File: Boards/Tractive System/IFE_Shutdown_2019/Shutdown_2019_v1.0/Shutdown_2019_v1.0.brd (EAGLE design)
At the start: 88.9 x 76.2 mm, 194 parts, among them Q1 DMN6140L-7, Q10 DMN6140L-7, Q11 DMP3099L-7, Q12 IRLML6346PBF, Q13 IRLML6346PBF, Q14 IRLML6346PBF, Q15 DMP3099L-7, Q16 DMN6140L-7, Q17 IRLML6346PBF, Q18 DMN6140L-7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

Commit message: Done with safety initial layout
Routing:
- net GND: track 0.00 -> 62.7 mm, vias 0 -> 128
- net +5V: track 241.0 -> 270.3 mm, vias 25 -> 27
- net +3V3: track 194.4 -> 219.4 mm, vias 13 -> 17
- net BRAKE_PRESSURE_F: track 4.22 -> 17.1 mm, vias 0 -> 2
- net DEBUG_TC: track 14.3 -> 15.1 mm
- net CURRENT_SENSE_F: track 35.2 -> 36.0 mm
- net BSPD_OC: track 13.2 -> 13.8 mm
- added copper zone on layer 1, net GND
- added copper zone on layer 16, net GND

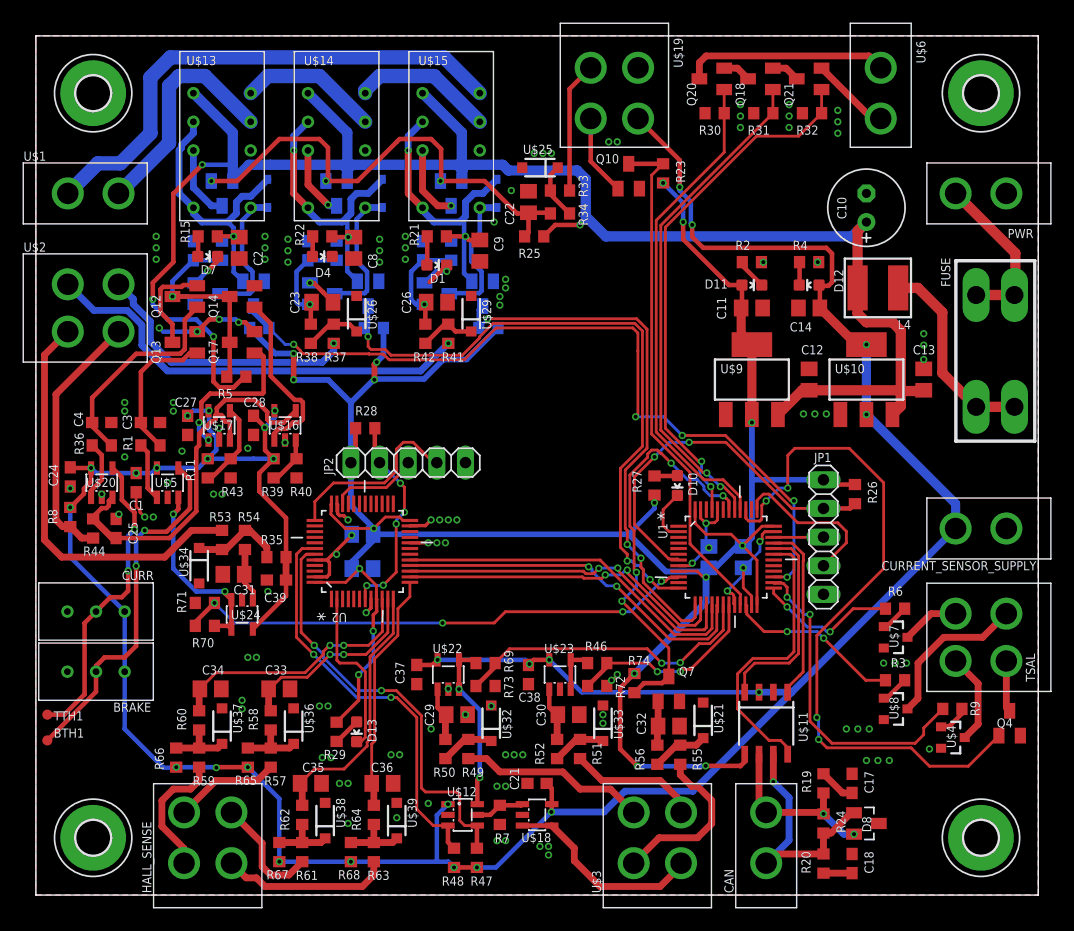
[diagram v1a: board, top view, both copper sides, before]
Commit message: Added rounded edges + Silk
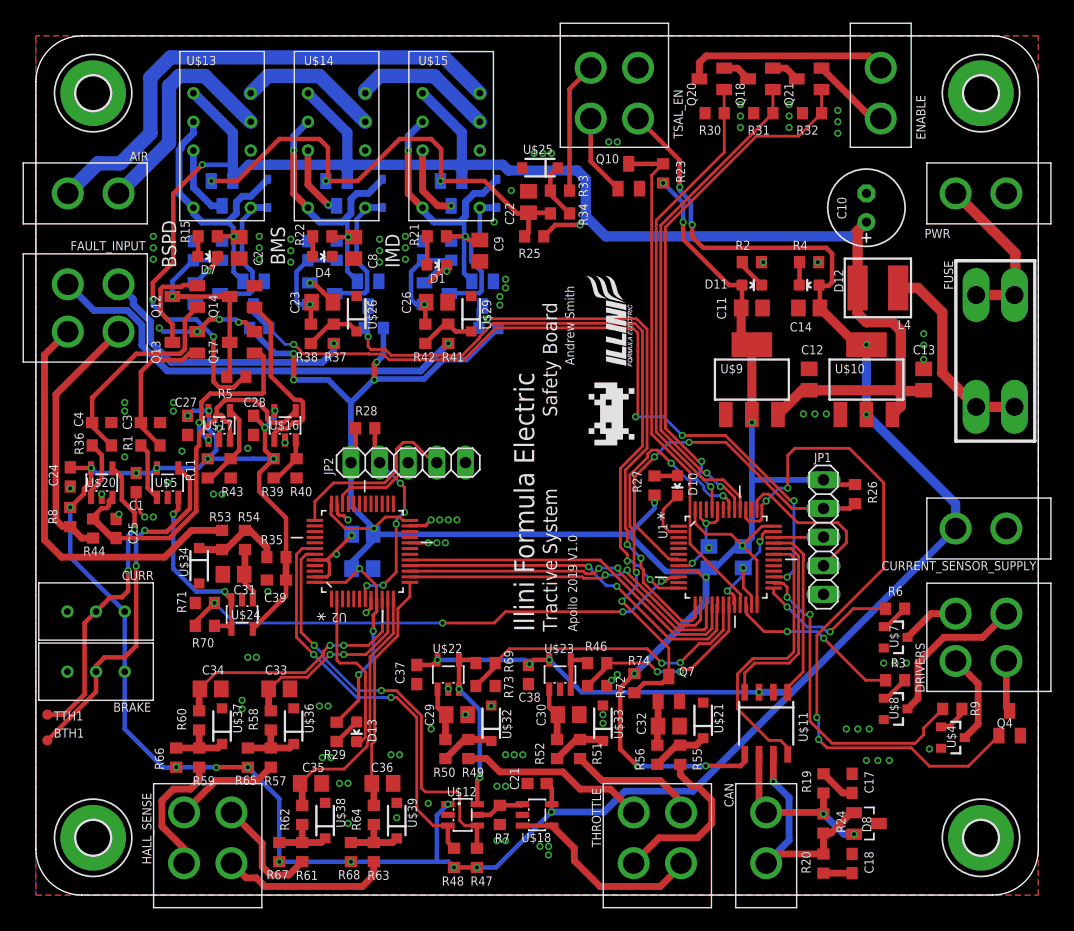
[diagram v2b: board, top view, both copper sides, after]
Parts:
- renumbered TSAL to DRIVERS, U$1 to AIR, U$19 to TSAL_EN, U$2 to FAULT_INPUT, U$3 to THROTTLE, U$6 to ENABLE
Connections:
- net HV_CONNECTED renamed TSAL_EN
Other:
- outline, holes or cut-outs redrawn
- board text added: "Andrew Smith"
- board text added: "Apollo 2019 V1.0"
- board text added: "BMS"
- board text added: "BSPD"
- board text added: "IMD"
- board text added: "Illini Formula Electric"
- board text added: "Safety Board"
- board text added: "Tractive System"

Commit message: fixing precharge + Shutdown
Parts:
- C21: value (none) -> 1u
- R2, R4: value (none) -> 100
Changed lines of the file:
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@@
 <setting verticaltext="up"/>
 </settings>
-<grid distance="20" unitdist="mil" unit="mil" style="lines" multiple="1" display="yes" altdistance="5" altunitdist="mil" altunit="mil"/>
+<grid distance="50" unitdist="mil" unit="mil" style="lines" multiple="1" display="no" altdistance="5" altunitdist="mil" altunit="mil"/>
 <layers>
 <layer number="1" name="Top" color="4" fill="1" visible="yes" active="yes"/>
@@
 <attribute name="NAME" x="85.217" y="14.859" size="0.8128" layer="25"/>
 </element>
-<element name="R4" library="rcl" library_urn="urn:adsk.eagle:library:334" package="R0603" package3d_urn="urn:adsk.eagle:package:23555/2" value="" x="68.58" y="56.134" smashed="yes" rot="R180">
+<element name="R4" library="rcl" library_urn="urn:adsk.eagle:library:334" package="R0603" package3d_urn="urn:adsk.eagle:package:23555/2" value="100" x="68.58" y="56.134" smashed="yes" rot="R180">
 <attribute name="NAME" x="68.453" y="58.039" size="0.8128" layer="25" rot="R180"/>
 <attribute name="SPICEPREFIX" value="R" x="68.58" y="56.134" size="1.778" layer="27" rot="R180" display="off"/>
 <attribute name="VALUE" x="69.215" y="58.039" size="1.27" layer="27" rot="R180"/>
 </element>
-<element name="R2" library="rcl" library_urn="urn:adsk.eagle:library:334" package="R0603" package3d_urn="urn:adsk.eagle:package:23555/2" value="" x="63.5" y="56.134" smashed="yes" rot="R180">
+<element name="R2" library="rcl" library_urn="urn:adsk.eagle:library:334" package="R0603" package3d_urn="urn:adsk.eagle:package:23555/2" value="100" x="63.5" y="56.134" smashed="yes" rot="R180">
 <attribute name="NAME" x="63.373" y="58.039" size="0.8128" layer="25" rot="R180"/>
 <attribute name="SPICEPREFIX" value="R" x="63.5" y="56.134" size="1.778" layer="27" rot="R180" display="off"/>
@@
 <attribute name="NAME" x="43.053" y="4.699" size="0.8128" layer="25"/>
 </element>
-<element name="C21" library="rcl" library_urn="urn:adsk.eagle:library:334" package="C0603" package3d_urn="urn:adsk.eagle:package:23616/2" value="" x="44.45" y="9.906" smashed="yes" rot="R180">
+<element name="C21" library="rcl" library_urn="urn:adsk.eagle:library:334" package="C0603" package3d_urn="urn:adsk.eagle:package:23616/2" value="1u" x="44.45" y="9.906" smashed="yes" rot="R180">
 <attribute name="NAME" x="42.037" y="11.303" size="0.8128" layer="25" rot="R270"/>
 <attribute name="SPICEPREFIX" value="C" x="44.45" y="9.906" size="1.778" layer="27" rot="R180" display="off"/>
